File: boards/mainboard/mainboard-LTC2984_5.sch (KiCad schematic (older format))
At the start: 33 parts, among them U601 LTC2984

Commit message: [mainboard] layout: footprints assigned, first placement
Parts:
- R602: footprint Resistors_ThroughHole:Resistor_Horizontal_RM7mm -> Resistors_THT:R_Axial_DIN0204_L3.6mm_D1.6mm_P5.08mm_Horizontal
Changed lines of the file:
@@
 F 0 "R602" V 4350 2200 50  0000 C CNN
 F 1 "2k00" V 4450 2200 50  0000 C CNN
-F 2 "Resistors_ThroughHole:Resistor_Horizontal_RM7mm" V 4380 2200 50  0001 C CNN
+F 2 "Resistors_THT:R_Axial_DIN0204_L3.6mm_D1.6mm_P5.08mm_Horizontal" V 4380 2200 50  0001 C CNN
 F 3 "" H 4450 2200 50  0000 C CNN
 	1    4450 2200
@@
 $EndComp
 $Comp
-L GND #PWR056
+L GND #PWR054
 U 1 1 58FFF541
 P 5650 1600
-F 0 "#PWR056" H 5650 1350 50  0001 C CNN
+F 0 "#PWR054" H 5650 1350 50  0001 C CNN
 F 1 "GND" H 5650 1450 50  0000 C CNN
 F 2 "" H 5650 1600 50  0000 C CNN
@@
 $EndComp
 $Comp
-L GND #PWR057
+L GND #PWR055
 U 1 1 58FFF581
 P 5650 4850
-F 0 "#PWR057" H 5650 4600 50  0001 C CNN
+F 0 "#PWR055" H 5650 4600 50  0001 C CNN
 F 1 "GND" H 5650 4700 50  0000 C CNN
 F 2 "" H 5650 4850 50  0000 C CNN
@@
 $EndComp
 $Comp
-L GND #PWR058
+L GND #PWR056
 U 1 1 58FFF584
 P 8200 1750
-F 0 "#PWR058" H 8200 1500 50  0001 C CNN
+F 0 "#PWR056" H 8200 1500 50  0001 C CNN
 F 1 "GND" H 8200 1600 50  0000 C CNN
 F 2 "" H 8200 1750 50  0000 C CNN
@@
 $EndComp
 $Comp
-L GND #PWR059
+L GND #PWR057
 U 1 1 58FFF58C
 P 7000 1150
-F 0 "#PWR059" H 7000 900 50  0001 C CNN
+F 0 "#PWR057" H 7000 900 50  0001 C CNN
 F 1 "GND" H 7000 1000 50  0000 C CNN
 F 2 "" H 7000 1150 50  0000 C CNN
@@
 $EndComp
 $Comp
-L GND #PWR060
+L GND #PWR058
 U 1 1 58FFF59E
 P 7100 5050
-F 0 "#PWR060" H 7100 4800 50  0001 C CNN
+F 0 "#PWR058" H 7100 4800 50  0001 C CNN
 F 1 "GND" H 7100 4900 50  0000 C CNN
 F 2 "" H 7100 5050 50  0000 C CNN
@@
 $EndComp
 $Comp
-L GND #PWR061
+L GND #PWR059
 U 1 1 587B8425
 P 7300 6150
-F 0 "#PWR061" H 7300 5900 50  0001 C CNN
+F 0 "#PWR059" H 7300 5900 50  0001 C CNN
 F 1 "GND" H 7300 6000 50  0000 C CNN
 F 2 "" H 7300 6150 50  0000 C CNN
@@
 $EndComp
 $Comp
-L GND #PWR062
+L GND #PWR060
 U 1 1 58FFF5B4
 P 7250 1250
-F 0 "#PWR062" H 7250 1000 50  0001 C CNN
+F 0 "#PWR060" H 7250 1000 50  0001 C CNN
 F 1 "GND" H 7250 1100 50  0000 C CNN
 F 2 "" H 7250 1250 50  0000 C CNN
@@
 $EndComp
 $Comp
-L GND #PWR063
+L GND #PWR061
 U 1 1 58FFF5BF
 P 7650 1050
-F 0 "#PWR063" H 7650 800 50  0001 C CNN
+F 0 "#PWR061" H 7650 800 50  0001 C CNN
 F 1 "GND" H 7650 900 50  0000 C CNN
 F 2 "" H 7650 1050 50  0000 C CNN
@@
 $EndComp
 $Comp
-L GND #PWR064
+L GND #PWR062
 U 1 1 58FFF5C7
 P 6550 4600
-F 0 "#PWR064" H 6550 4350 50  0001 C CNN
+F 0 "#PWR062" H 6550 4350 50  0001 C CNN
 F 1 "GND" H 6550 4450 50  0000 C CNN
 F 2 "" H 6550 4600 50  0000 C CNN
@@
 VREF_BYP
 $Comp
-L +3V3 #PWR065
+L +3V3 #PWR063
 U 1 1 58FFF5CB
 P 7500 5050
-F 0 "#PWR065" H 7500 4900 50  0001 C CNN
+F 0 "#PWR063" H 7500 4900 50  0001 C CNN
 F 1 "+3V3" H 7500 5190 50  0000 C CNN
 F 2 "" H 7500 5050 50  0000 C CNN
@@
 $EndComp
 $Comp
-L +3V3 #PWR066
+L +3V3 #PWR064
 U 1 1 58FFF5CD
 P 7300 5450
-F 0 "#PWR066" H 7300 5300 50  0001 C CNN
+F 0 "#PWR064" H 7300 5300 50  0001 C CNN
 F 1 "+3V3" H 7300 5590 50  0000 C CNN
 F 2 "" H 7300 5450 50  0000 C CNN
@@
 	4300 2000 4250 2000
 $Comp
-L +3V3 #PWR067
+L +3V3 #PWR065
 U 1 1 58FFF5D8
 P 9050 3400
-F 0 "#PWR067" H 9050 3250 50  0001 C CNN
+F 0 "#PWR065" H 9050 3250 50  0001 C CNN
 F 1 "+3V3" H 9050 3540 50  0000 C CNN
 F 2 "" H 9050 3400 50  0000 C CNN
@@
 $EndComp
 $Comp
-L +3V3 #PWR068
+L +3V3 #PWR066
 U 1 1 58FFF5EE
 P 8550 1900
-F 0 "#PWR068" H 8550 1750 50  0001 C CNN
+F 0 "#PWR066" H 8550 1750 50  0001 C CNN
 F 1 "+3V3" H 8550 2040 50  0000 C CNN
 F 2 "" H 8550 1900 50  0000 C CNN

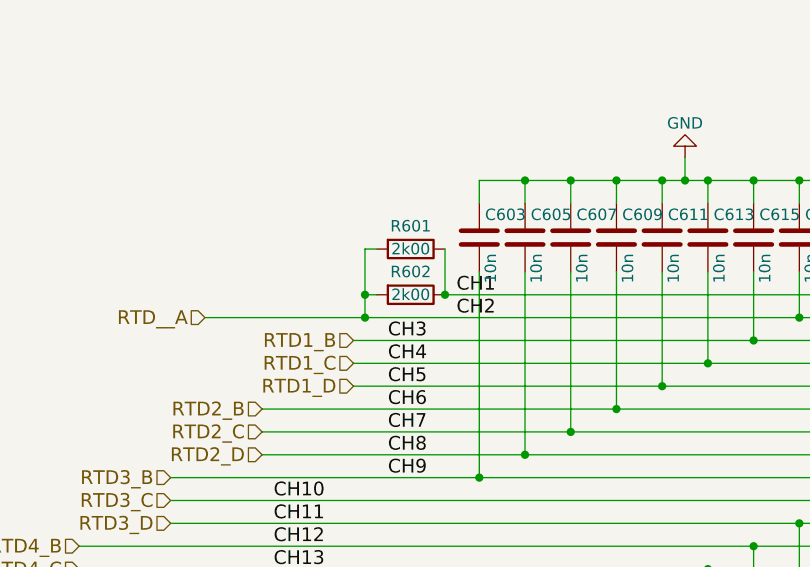
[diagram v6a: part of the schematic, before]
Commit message: [mainboard] first traces routed, some pins in schematic swapped
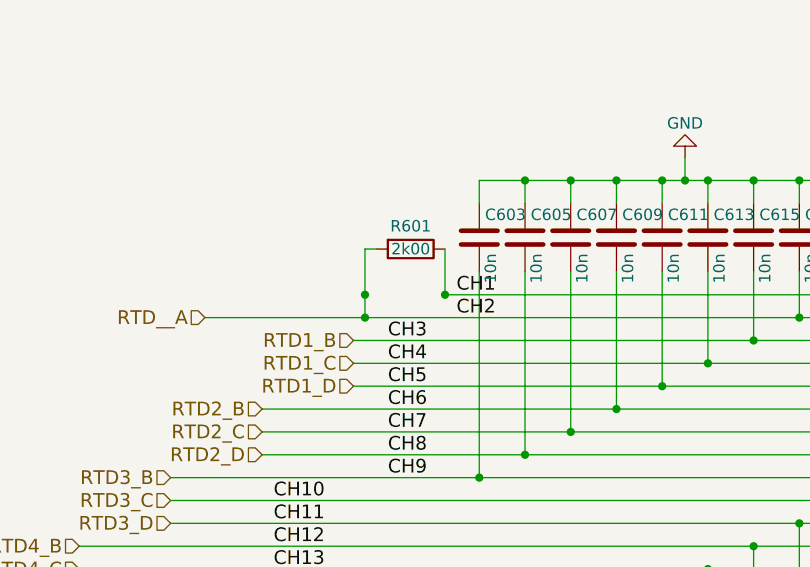
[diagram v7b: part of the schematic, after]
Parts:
- removed R602: 2k00, Resistors_THT:R_Axial_DIN0204_L3.6mm_D1.6mm_P5.08mm_Horizontal, symbol R
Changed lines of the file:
@@
-$EndComp
-$Comp
-L R R602
-U 1 1 58FFF512
-P 4450 2200
-F 0 "R602" V 4350 2200 50  0000 C CNN
-F 1 "2k00" V 4450 2200 50  0000 C CNN
-F 2 "Resistors_THT:R_Axial_DIN0204_L3.6mm_D1.6mm_P5.08mm_Horizontal" V 4380 2200 50  0001 C CNN
-F 3 "" H 4450 2200 50  0000 C CNN
-	1    4450 2200
-	0    1    1    0
 $EndComp
 $Comp
@@
 Wire Wire Line
 	9050 3400 8950 3400
-Wire Wire Line
-	4250 2200 4300 2200
 Text HLabel 4200 2400 0    60   Input ~ 0
 RTD1_B
